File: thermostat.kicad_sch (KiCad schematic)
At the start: 79 parts, among them U17 AD5680, U18 AD7172-2, U19 RS8552, U20 MAX1968xUI

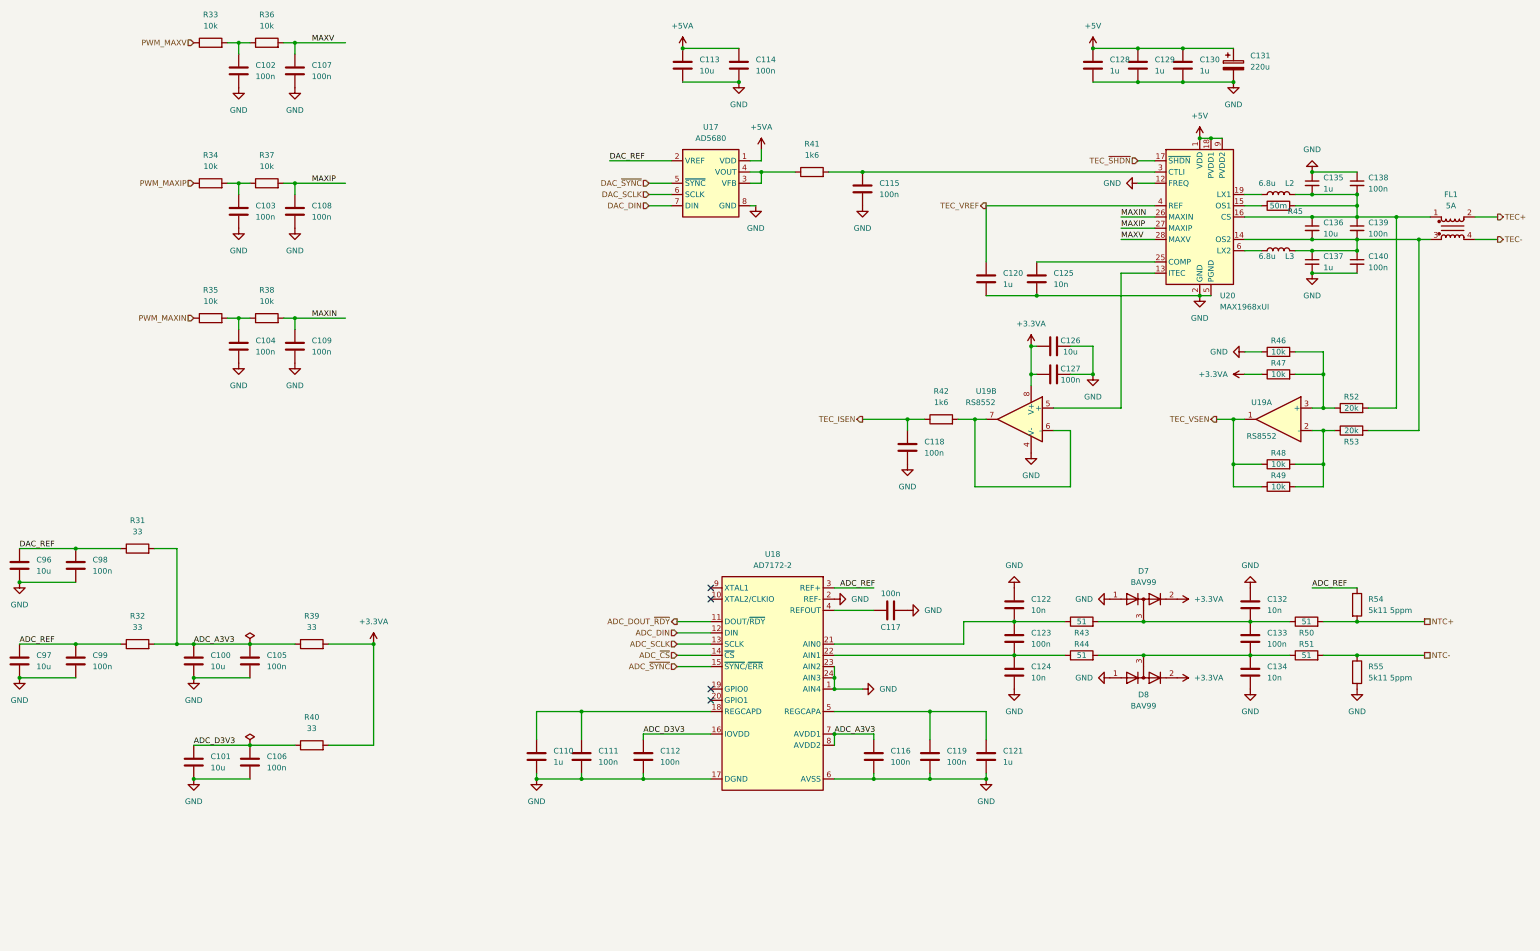
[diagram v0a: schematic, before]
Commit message: Complete BOM, FP assignment
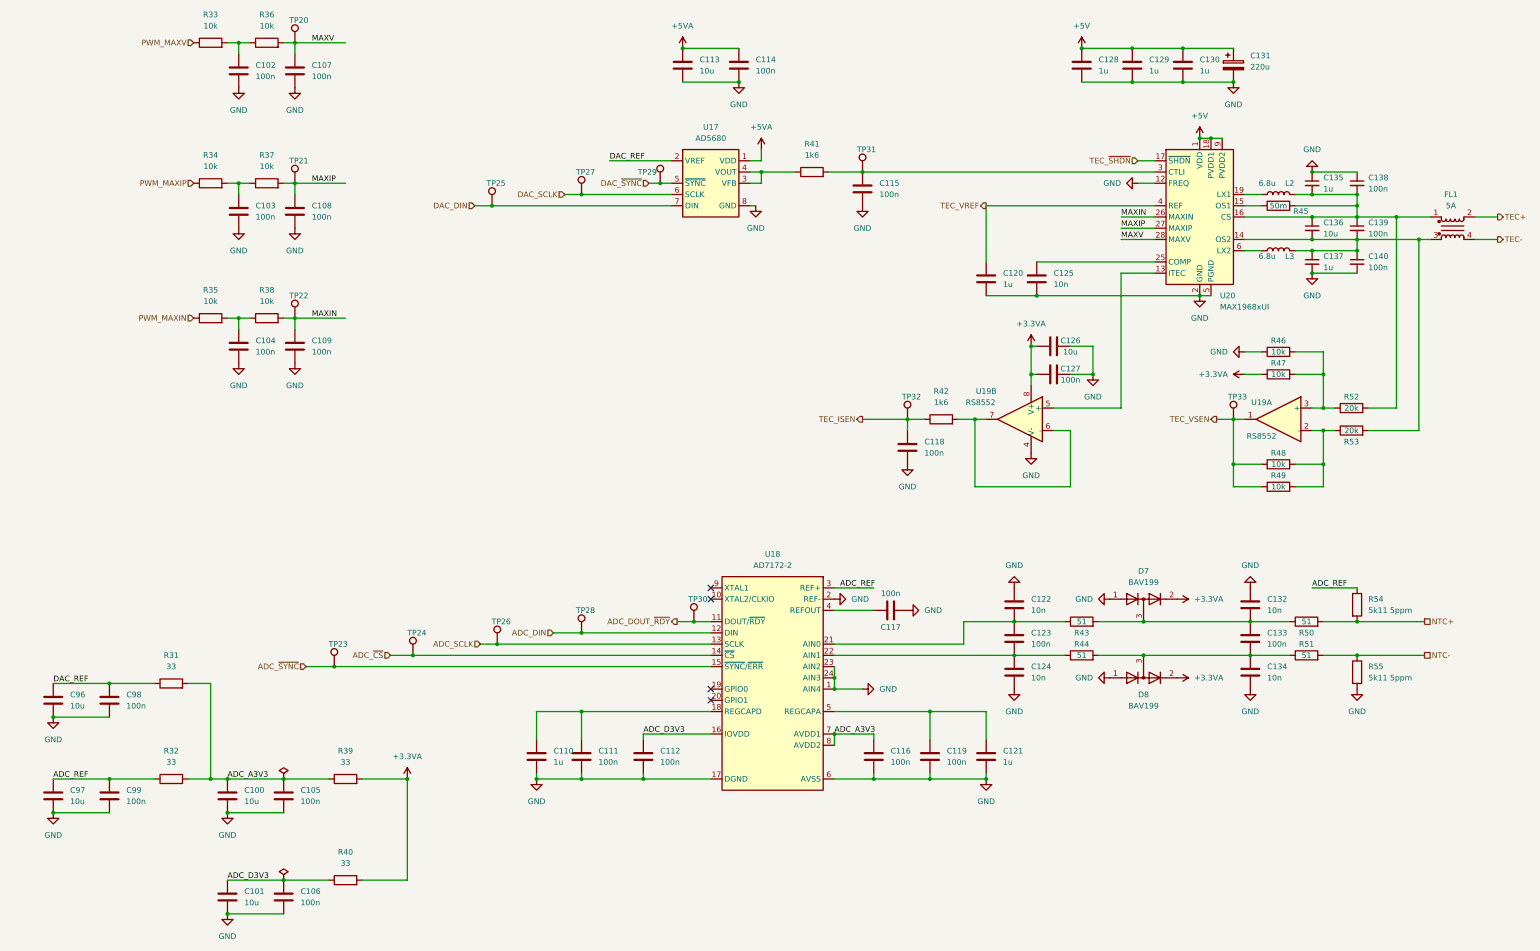
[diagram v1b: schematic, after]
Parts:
- added TP20, TP21, TP22, TP23, TP24, TP25, TP26, TP27, TP28, TP29, TP30, TP31, TP32, TP33: TestPoint, TestPoint:TestPoint_Pad_2.0x2.0mm, symbol Connector:TestPoint
- C100, C101, C113, C126, C136, C96, C97: footprint (none) -> Capacitor_SMD:C_0805_2012Metric; MFR_PN (none) -> CL21B106KOQNNNG; MFR_PN_ALT (none) -> CL21B106KOQNNNE
- C102, C103, C104, C105, C106, C107, C108, C109, C111, C112, C114, C115, C116, C117, C118, C119, C123, C127, C133, C138, C139, C140, C98, C99: footprint (none) -> Capacitor_SMD:C_0603_1608Metric; MFR_PN (none) -> CL10B104KB8NNWC; MFR_PN_ALT (none) -> CL10B104KB8NNNL
- C110, C120, C121, C128, C129, C130, C135, C137: footprint (none) -> Capacitor_SMD:C_0603_1608Metric; MFR_PN (none) -> CL10B105KA8NNNC; MFR_PN_ALT (none) -> CGA3E1X7R1E105K080AC
- C122, C124, C125, C132, C134: footprint (none) -> Capacitor_SMD:C_0603_1608Metric; MFR_PN (none) -> 0603B103K500CT; MFR_PN_ALT (none) -> CL10B103KB8NNNC
- C131: footprint (none) -> Capacitor_Tantalum_SMD:CP_EIA-7343-15_Kemet-W; MFR_PN (none) -> T491D227K016AT; MFR_PN_ALT (none) -> 293D227X9016E2TE3
- D7, D8: value BAV99 -> BAV199; MFR_PN (none) -> BAV199W-7; MFR_PN_ALT (none) -> BAV199E6327HTSA1
- FL1: footprint (none) -> Inductor_SMD:L_CommonModeChoke_Wuerth_WE-SL5; MFR_PN (none) -> 744273501
- L2, L3: footprint (none) -> Inductor_SMD:L_Wuerth_MAPI-4030; MFR_PN (none) -> 74438357068
- R31, R32, R39, R40: footprint (none) -> Resistor_SMD:R_0603_1608Metric; MFR_PN (none) -> RC0603FR-0733RL; MFR_PN_ALT (none) -> CRGCQ0603F33R
- R33, R34, R35, R36, R37, R38, R46, R47, R48, R49: footprint (none) -> Resistor_SMD:R_0603_1608Metric; MFR_PN (none) -> RNCP0603FTD10K0; MFR_PN_ALT (none) -> RMCF0603FT10K0
- R41, R42: footprint (none) -> Resistor_SMD:R_0603_1608Metric; MFR_PN (none) -> RT0603FRE071K6L; MFR_PN_ALT (none) -> RMCF0603FT1K60
- R43, R44, R50, R51: footprint (none) -> Resistor_SMD:R_0603_1608Metric; MFR_PN (none) -> ESR03EZPF51R0; MFR_PN_ALT (none) -> RMCF0603FT51R0
- R45: footprint (none) -> Resistor_SMD:R_2010_5025Metric; MFR_PN (none) -> WSL2010R5000FEA18; MFR_PN_ALT (none) -> WSLT2010R5000FEA18
- R52, R53: footprint (none) -> Resistor_SMD:R_0603_1608Metric; MFR_PN (none) -> RMCF0603FT20K0; MFR_PN_ALT (none) -> RC0603FR-0720KL
- R54, R55: footprint (none) -> Resistor_SMD:R_0603_1608Metric; MFR_PN (none) -> RN73H1JTTD5111A05; MFR_PN_ALT (none) -> TNPU06035K11BZEN00
- U17: MFR_PN (none) -> AD5680BRJZ
- U18: MFR_PN (none) -> AD7172-2BRUZ
- U19: MFR_PN (none) -> RS8552XK
- U20: MFR_PN (none) -> MAX1968EUI+; MFR_PN_ALT (none) -> MAX1968EUI+T
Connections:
- net ADC_DIN: now also TP28.1
- net ADC_DOUT_~{RDY}: now also TP30.1
- net ADC_SCLK: now also TP26.1
- net ADC_~{CS}: now also TP24.1
- net ADC_~{SYNC}: now also TP23.1
- net DAC_DIN: now also TP25.1
- net DAC_SCLK: now also TP27.1
- net DAC_~{SYNC}: now also TP29.1
- net MAXIN: now also TP22.1
- net MAXIP: now also TP21.1
- net MAXV: now also TP20.1
- net TEC_ISEN: now also TP32.1
- net TEC_VSEN: now also TP33.1
- net at C115.1, R41.2, U20.3 (CTLI): now also TP31.1
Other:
- moved on the sheet: C100, C101, C105, C106, C128, C129, C96, C97, C98, C99, R31, R32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

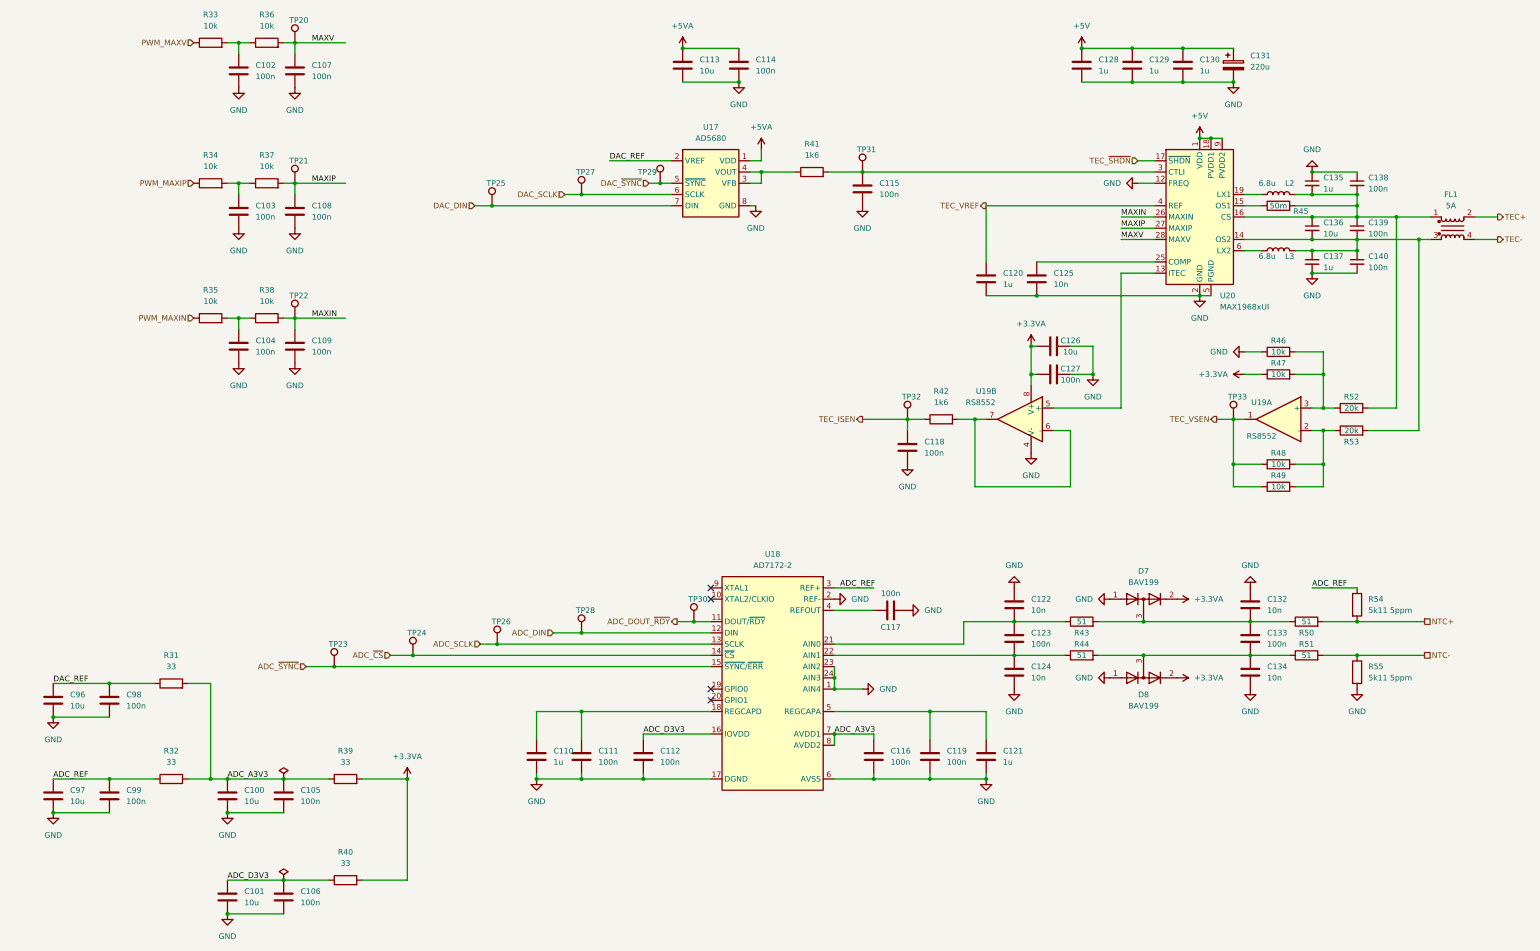
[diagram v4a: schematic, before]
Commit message: import sch to pcb
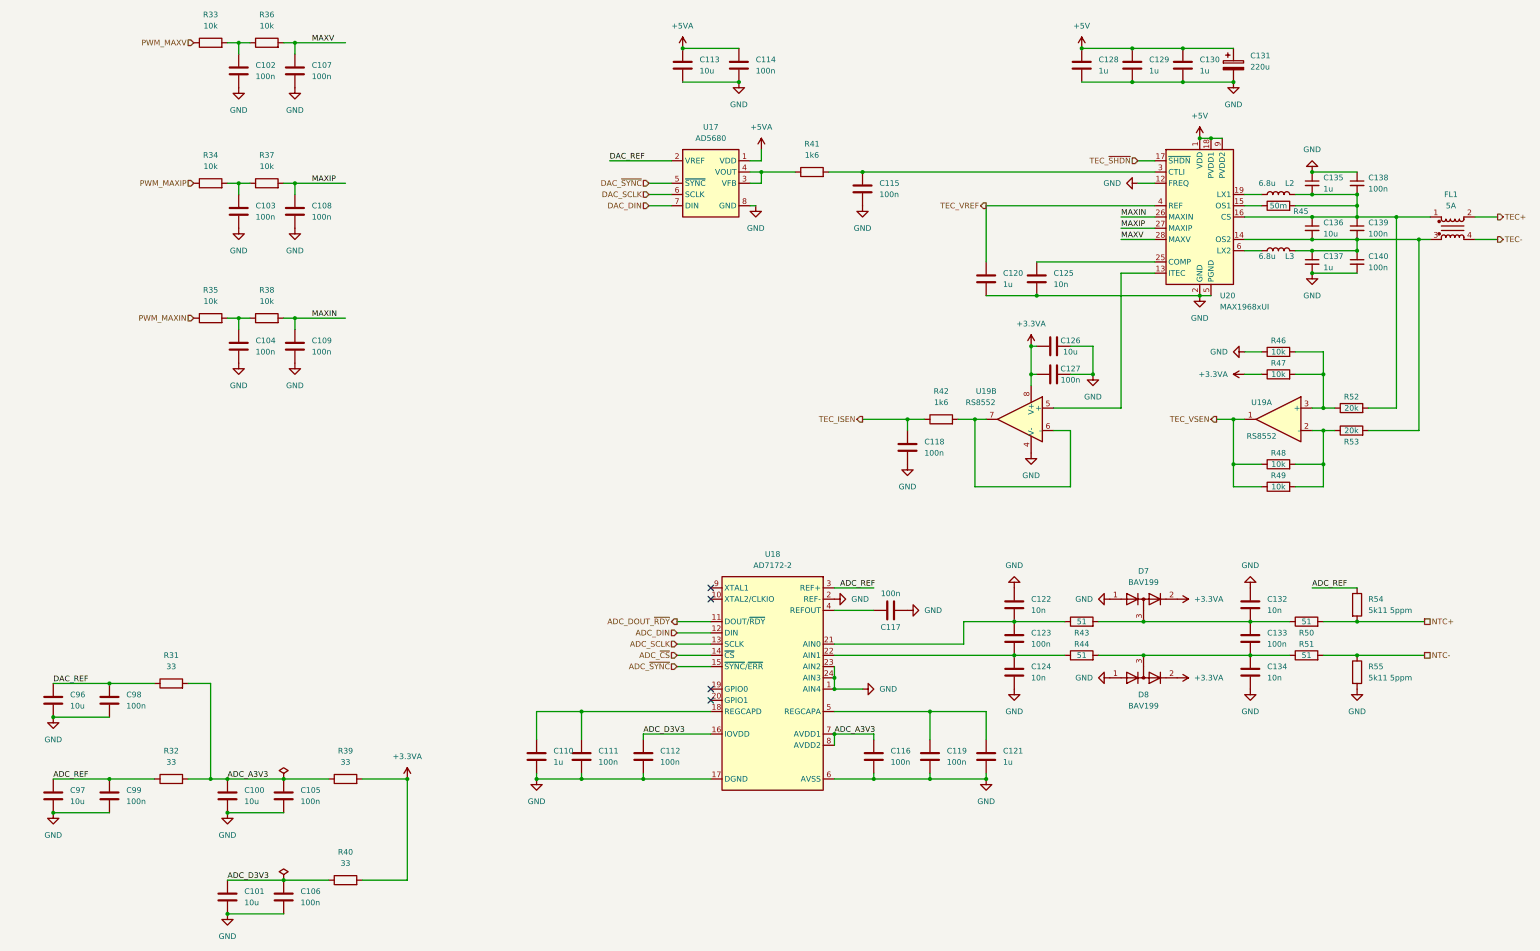
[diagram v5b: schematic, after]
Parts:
- removed TP20, TP21, TP22, TP23, TP24, TP25, TP26, TP27, TP28, TP29, TP30, TP31, TP32, TP33: TestPoint, TestPoint:TestPoint_Pad_2.0x2.0mm, symbol Connector:TestPoint

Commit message: sync
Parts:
- removed FL1: 5A, Inductor_SMD:L_CommonModeChoke_Wuerth_WE-SL5, symbol Device:Filter_EMI_CommonMode
- added FL1: 5A, Inductor_SMD:L_CommonModeChoke_Wuerth_WE-SL5, symbol Device:Filter_EMI_LL_1423
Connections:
- net TEC+: now also FL1.4
- net TEC-: now also FL1.3
- net at C135.2, C136.1, C138.2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: now also FL1.1
- net at C136.2, C137.1, C139.2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: now also FL1.2
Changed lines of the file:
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@@
     (pin "2")
+  )
+  (symbol (lib_id "Device:Filter_EMI_LL_1423") (at 358.14 104.14 0) (mirror x) (unit 1)
+    (in_bom yes) (on_board yes) (fields_autoplaced)
+    (property "Reference" "FL1" (id 0) (at 357.759 96.52 0))
+    (property "Value" "5A" (id 1) (at 357.759 99.06 0))
+    (property "Footprint" "Inductor_SMD:L_CommonModeChoke_Wuerth_WE-SL5" (id 2) (at 358.14 97.79 0)
+      (effects (font (size 1.27 1.27)) hide)
+    )
+    (property "Datasheet" "~" (id 3) (at 358.14 105.156 90)
+      (effects (font (size 1.27 1.27)) hide)
+    )
+    (property "MFR_PN" "744273501" (id 4) (at 358.14 104.14 0)
+      (effects (font (size 1.27 1.27)) hide)
+    )
+    (pin "1")
+    (pin "2")
+    (pin "3")
+    (pin "4")
   )
   (symbol (lib_id "power:+3.3VA") (at 295.91 187.96 270) (unit 1)
@@
     (pin "2")
   )
-  (symbol (lib_id "Device:Filter_EMI_CommonMode") (at 358.14 104.14 0) (unit 1)
-    (in_bom yes) (on_board yes) (fields_autoplaced)
-    (property "Reference" "FL1" (id 0) (at 357.759 96.52 0))
-    (property "Value" "5A" (id 1) (at 357.759 99.06 0))
-    (property "Footprint" "Inductor_SMD:L_CommonModeChoke_Wuerth_WE-SL5" (id 2) (at 358.14 103.124 0)
-      (effects (font (size 1.27 1.27)) hide)
-    )
-    (property "Datasheet" "~" (id 3) (at 358.14 103.124 0)
-      (effects (font (size 1.27 1.27)) hide)
-    )
-    (property "MFR_PN" "744273501" (id 4) (at 358.14 104.14 0)
-      (effects (font (size 1.27 1.27)) hide)
-    )
-    (pin "1")
-    (pin "2")
-    (pin "3")
-    (pin "4")
-  )
   (symbol (lib_id "Device:C") (at 231.14 190.5 90) (unit 1)

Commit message: update palcement
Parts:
- FL1: value 5A -> 2x1m
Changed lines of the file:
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@@
     (pin "2")
+  )
+  (symbol (lib_id "Device:Filter_EMI_LL_1423") (at 358.14 104.14 0) (mirror x) (unit 1)
+    (in_bom yes) (on_board yes) (fields_autoplaced)
+    (property "Reference" "FL1" (id 0) (at 357.759 96.52 0))
+    (property "Value" "2x1m" (id 1) (at 357.759 99.06 0))
+    (property "Footprint" "Inductor_SMD:L_CommonModeChoke_Wuerth_WE-SL5" (id 2) (at 358.14 97.79 0)
+      (effects (font (size 1.27 1.27)) hide)
+    )
+    (property "Datasheet" "~" (id 3) (at 358.14 105.156 90)
+      (effects (font (size 1.27 1.27)) hide)
+    )
+    (property "MFR_PN" "744273501" (id 4) (at 358.14 104.14 0)
+      (effects (font (size 1.27 1.27)) hide)
+    )
+    (pin "1")
+    (pin "2")
+    (pin "3")
+    (pin "4")
   )
   (symbol (lib_id "Device:R") (at 318.77 132.08 90) (unit 1)
@@
     (pin "2")
   )
-  (symbol (lib_id "Device:Filter_EMI_LL_1423") (at 358.14 104.14 0) (mirror x) (unit 1)
-    (in_bom yes) (on_board yes) (fields_autoplaced)
-    (property "Reference" "FL1" (id 0) (at 357.759 96.52 0))
-    (property "Value" "5A" (id 1) (at 357.759 99.06 0))
-    (property "Footprint" "Inductor_SMD:L_CommonModeChoke_Wuerth_WE-SL5" (id 2) (at 358.14 97.79 0)
-      (effects (font (size 1.27 1.27)) hide)
-    )
-    (property "Datasheet" "~" (id 3) (at 358.14 105.156 90)
-      (effects (font (size 1.27 1.27)) hide)
-    )
-    (property "MFR_PN" "744273501" (id 4) (at 358.14 104.14 0)
-      (effects (font (size 1.27 1.27)) hide)
-    )
-    (pin "1")
-    (pin "2")
-    (pin "3")
-    (pin "4")
-  )
   (symbol (lib_id "power:+3.3VA") (at 295.91 187.96 270) (unit 1)

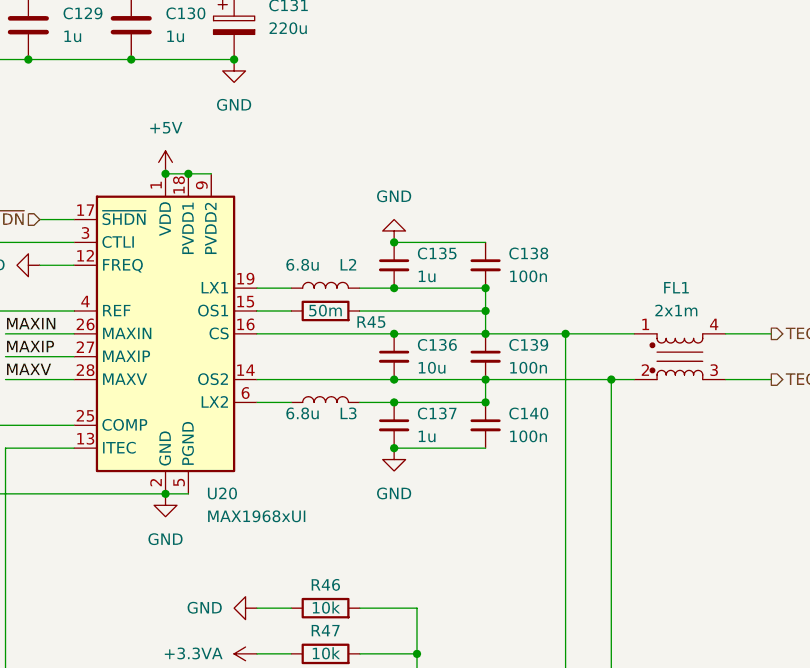
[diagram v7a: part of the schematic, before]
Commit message: finish v2 layout
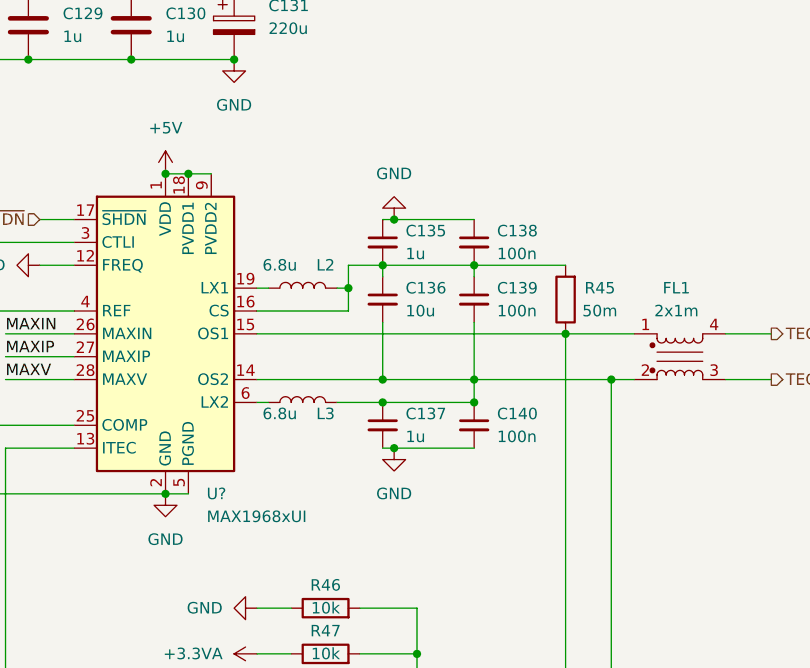
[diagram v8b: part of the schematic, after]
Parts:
- removed U20: MAX1968xUI, Package_SO:HTSSOP-28-1EP_4.4x9.7mm_P0.65mm_EP2.85x5.4mm, symbol Driver_TEC:MAX1968xUI
- added U?: MAX1968xUI, Package_SO:HTSSOP-28-1EP_4.4x9.7mm_P0.65mm_EP2.85x5.4mm, symbol kirdy:MAX1968xUI
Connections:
- net +5V: now also U?.1 (VDD), U?.11 (PVDD2), U?.18 (PVDD1), U?.20 (PVDD1), U?.9 (PVDD2)
- net GND: now also U?.12 (FREQ), U?.2 (GND), U?.22 (PGND), U?.24 (PGND), U?.29 (GND), U?.5 (PGND), U?.7 (PGND)
- net MAXIN: now also U?.26 (MAXIN)
- net MAXIP: now also U?.27 (MAXIP)
- net MAXV: now also U?.28 (MAXV)
- net TEC_VREF: now also U?.4 (REF)
- net TEC_~{SHDN}: now also U?.17 (~{SHDN})
- net at R45.1: now also FL1.1, R52.2, U?.15 (OS1)
- net at C135.2, C136.1, C138.2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: now also U?.16 (CS); no longer FL1.1, R52.2
- net at C136.2, C137.1, C139.2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: now also U?.14 (OS2)
- net at L3.1: now also U?.10 (LX2), U?.6 (LX2), U?.8 (LX2)
- net at C115.1, R41.2: now also U?.3 (CTLI)
- net at L2.1: now also U?.19 (LX1), U?.21 (LX1), U?.23 (LX1)
- net at U19.5 (+): now also U?.13 (ITEC)
- net at C125.1: now also U?.25 (COMP)
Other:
- moved on the sheet: C135, C136, C137, C138, C139, C140, L2, L3, R45
